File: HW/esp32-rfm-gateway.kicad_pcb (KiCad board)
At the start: 2 copper layers, 99 x 93.5 mm, 66 parts, among them J1 Res, J2 Boot, J20 220V~, J21 c5V, J22 s14500, J23 s18650, J24 cPS, J25 c3V3, J3 PinDbg, J30 AntSMA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

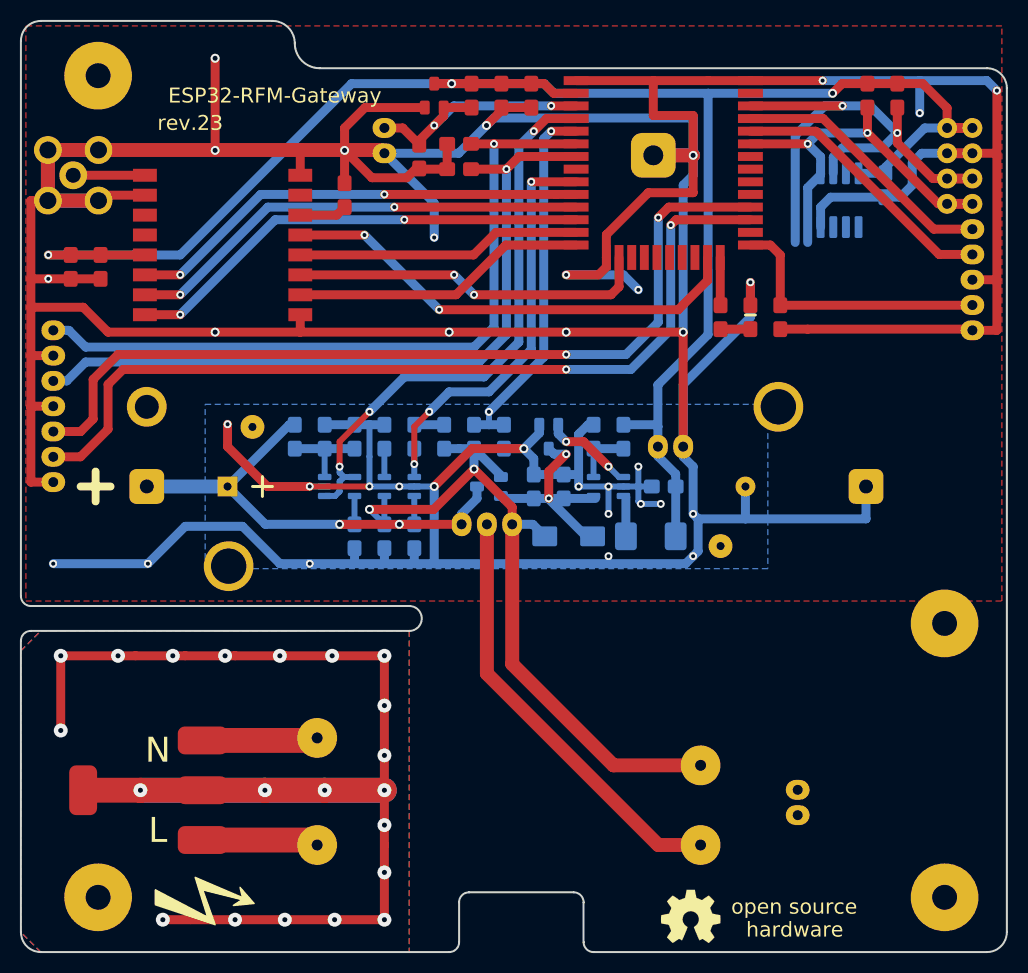
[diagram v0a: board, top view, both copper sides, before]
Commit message: Adds 4 LEDs, resistor and light pipes. The LEDs are NOT controlled yet !
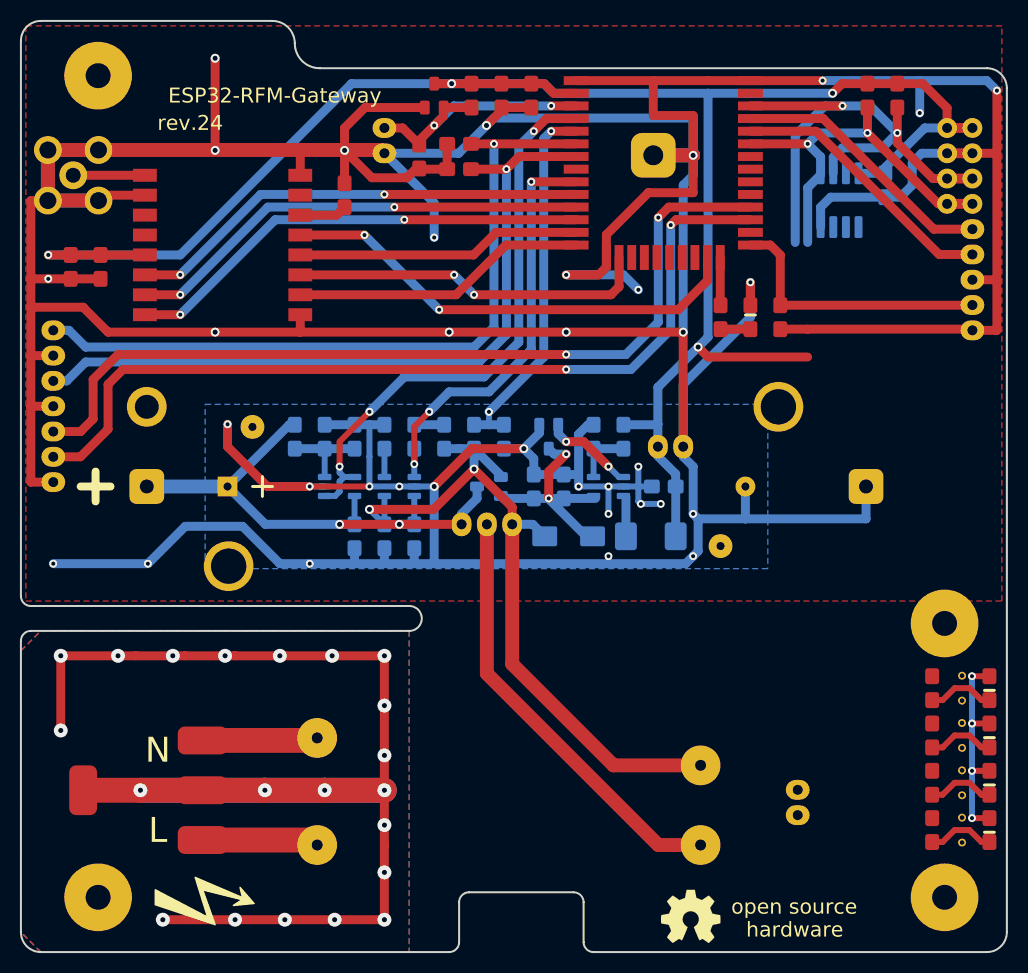
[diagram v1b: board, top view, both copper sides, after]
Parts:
- added D10: LED, CalinGeneric:LED0805HS, F.Cu at (133.2, 125.0)
- added D11: LED, CalinGeneric:LED0805HS, F.Cu at (133.2, 120.2)
- added D12: LED, CalinGeneric:LED0805HS, F.Cu at (133.2, 115.5)
- added D13: LED, CalinGeneric:LED0805HS, F.Cu at (133.2, 110.8)
- added R10: 100, CalinGeneric:R0805HS, F.Cu at (127.5, 125.0)
- added R11: 100, CalinGeneric:R0805HS, F.Cu at (127.5, 120.2)
- added R12: 100, CalinGeneric:R0805HS, F.Cu at (127.5, 115.5)
- added R13: 100, CalinGeneric:R0805HS, F.Cu at (127.5, 110.8)
- added SYM10: LightPipe, CalinGeneric:SLP3-xxx-150-x, F.Cu at (130.5, 125.0)
- added SYM11: LightPipe, CalinGeneric:SLP3-xxx-150-x, F.Cu at (130.5, 120.2)
- added SYM12: LightPipe, CalinGeneric:SLP3-xxx-150-x, F.Cu at (130.5, 115.5)
- added SYM13: LightPipe, CalinGeneric:SLP3-xxx-150-x, F.Cu at (130.5, 110.8)
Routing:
- net +3V3: track 190.1 -> 222.7 mm, vias 3 -> 8
- net Net-(D13-PadK): track 0.00 -> 6.74 mm
- net Net-(D12-PadK): track 0.00 -> 6.74 mm
- net Net-(D11-PadK): track 0.00 -> 6.74 mm
- net Net-(D10-PadK): track 0.00 -> 6.74 mm
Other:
- board text added: "rev.24"
- board text removed: "rev.23"

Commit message: Changes to schematic to a hierarchical one
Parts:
- J1: value Res -> ph_1x2
- J2: value Boot -> ph_1x2
- J21: value c5V -> ph_1x2
- J24: value cPS -> ph_1x3
- J25: value c3V3 -> ph_1x2
- J3: value PinDbg -> ph_1x3
- J4, J5: value PinsI2C -> ph_1x4
- J6: value PinsUSART2 -> ph_1x3
- J7: value ExtButtons -> ph_1x4
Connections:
- net /ACL renamed /Power Section/ACL
- net /ACN renamed /Power Section/ACN
- net /PwrSW renamed /Power Section/PwrSW
- net /VinReg renamed /Power Section/VinReg

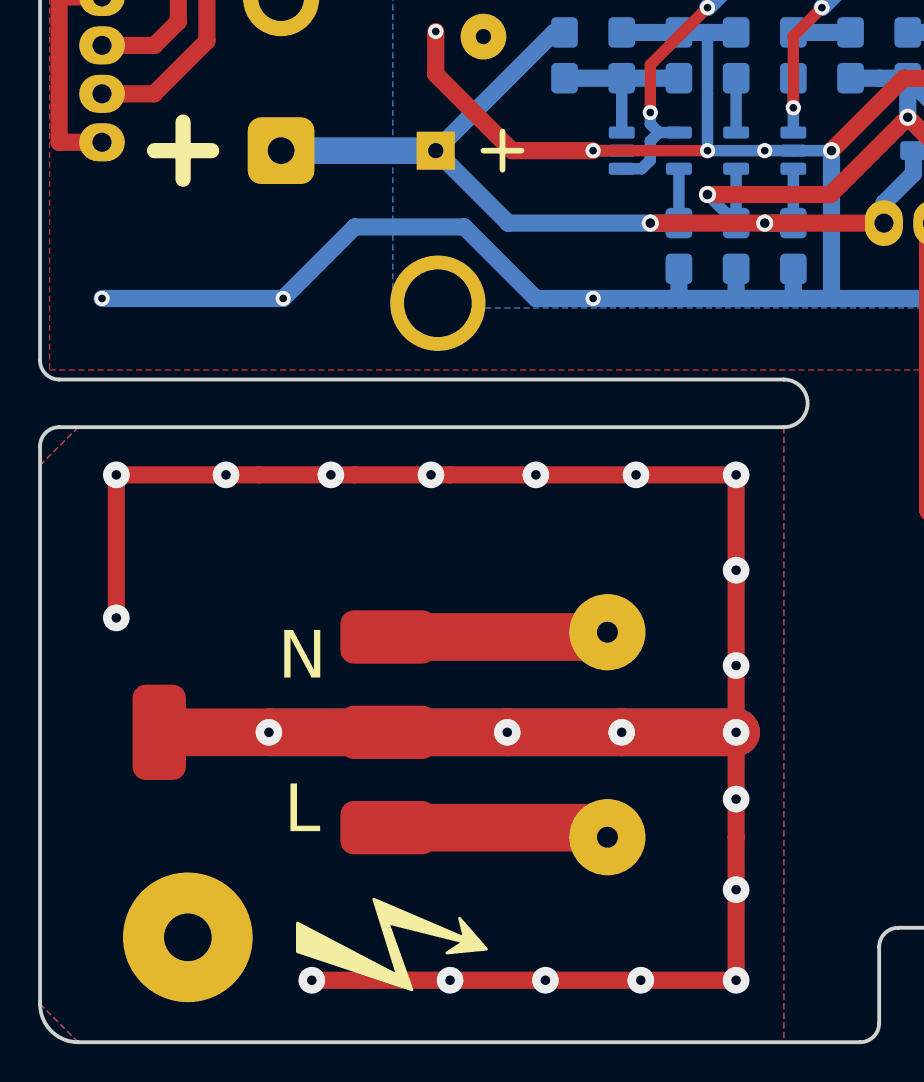
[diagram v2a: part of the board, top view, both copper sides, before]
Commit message: Changes the high-voltage section
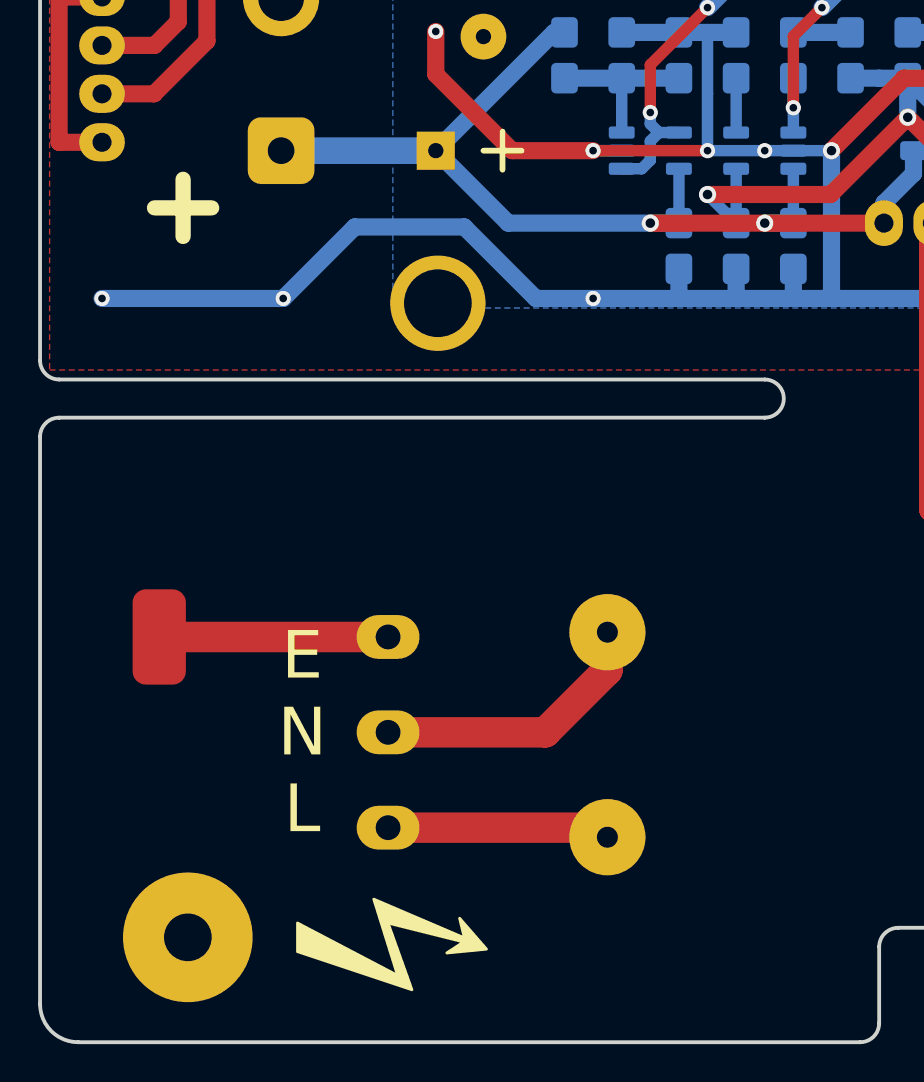
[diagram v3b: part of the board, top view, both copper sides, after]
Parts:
- J20: footprint CalinConnectors:SMD_Pins_Big_1x3 -> CalinConnectors:THT_Pins_Big_1x3
- moved H5 5.00 mm to (42.2, 116.0)
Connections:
- J20 pad 1: /Power Section/ACN -> Earth
- J20 pad 2: Earth -> /Power Section/ACN
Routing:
- net Earth: track 143.5 -> 12.0 mm, vias 21 -> 0
- net /Power Section/ACN: track 11.6 -> 14.8 mm
- removed copper zone on B.Cu, net Earth
- removed copper zone on F.Cu, net Earth
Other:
- outline, holes or cut-outs redrawn
- board text added: "E N L"
- board text removed: "N L"

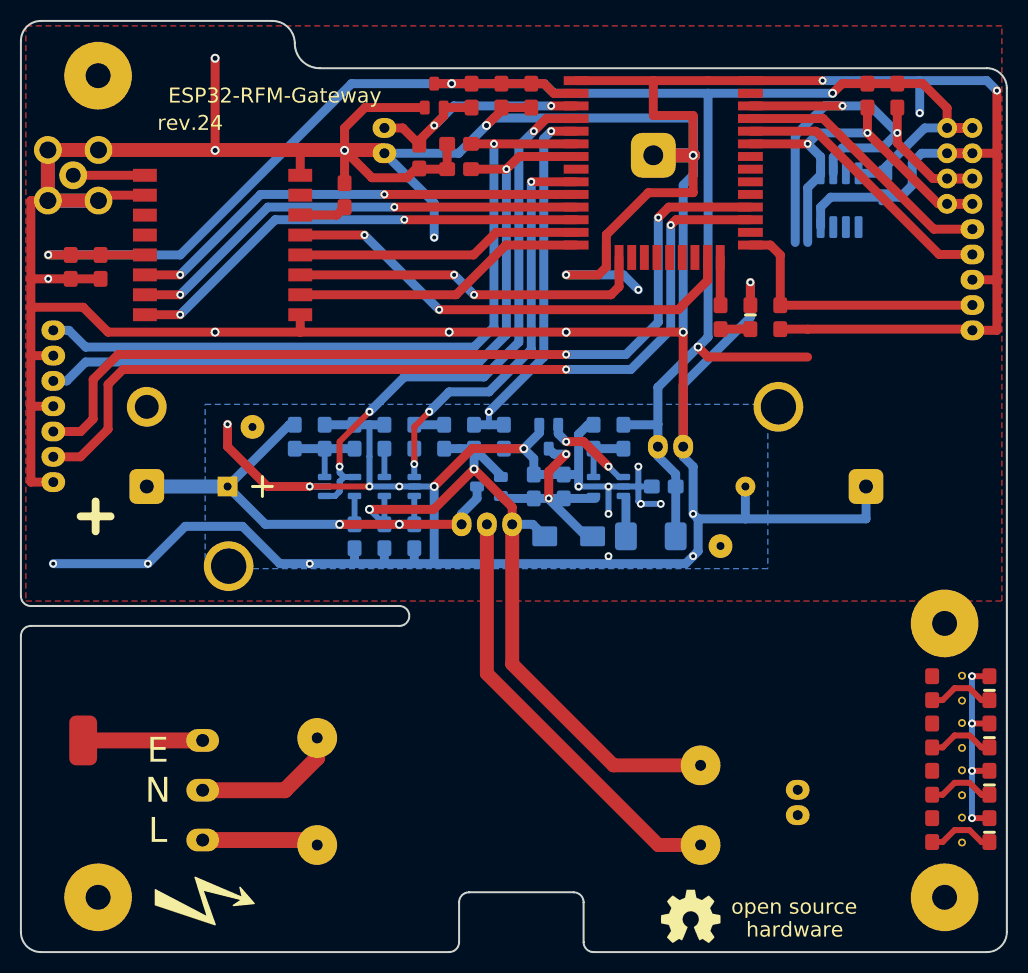
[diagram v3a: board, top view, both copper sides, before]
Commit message: Adds DTR and RTS connector and the components for automatic setting of EN and Boot signals
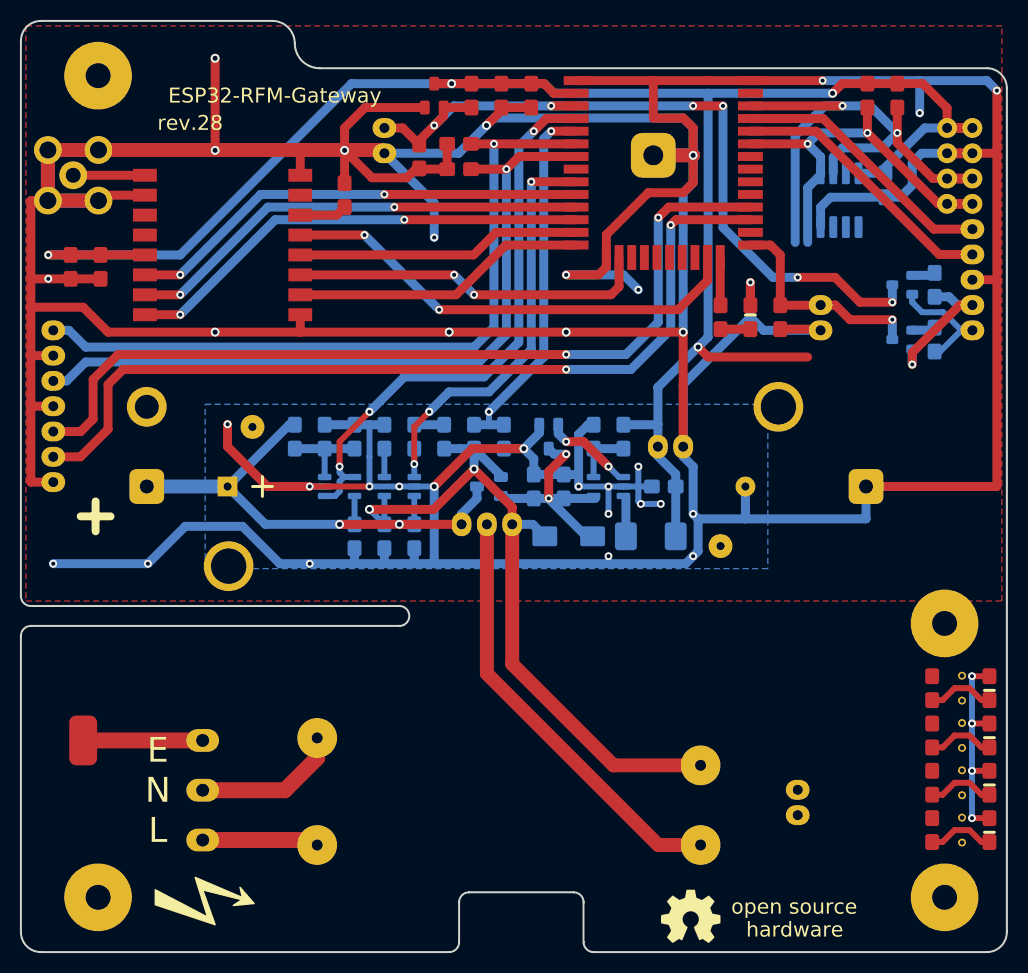
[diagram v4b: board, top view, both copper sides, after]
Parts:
- added J40: ph_1x2, CalinConnectors:Pin_Header_Straight_1x02, F.Cu at (131.5, 72.3)
- added Q40: BC817, CalinGeneric:SOT-23, B.Cu at (124.5, 70.2)
- added Q41: BC817, CalinGeneric:SOT-23, B.Cu at (124.5, 75.8)
- added R40: 10K, CalinGeneric:R0805HS, B.Cu at (127.8, 70.2)
- added R41: 10K, CalinGeneric:R0805HS, B.Cu at (127.8, 75.8)
- moved J2 15.2 mm to (116.3, 72.3)
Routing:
- net /Reset: track 26.8 -> 78.1 mm, vias 2 -> 6
- net GND: track 734.9 -> 751.9 mm
- net /Additional Modules/DTR: track 0.00 -> 14.9 mm, vias 0 -> 1
- net /Additional Modules/RTS: track 0.00 -> 11.6 mm
- net /Boot: track 27.8 -> 22.3 mm, vias 0 -> 1
- net Net-(Q41-Pad1): track 0.00 -> 2.35 mm
- net Net-(Q40-Pad1): track 0.00 -> 2.35 mm
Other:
- board text added: "rev.28"
- board text removed: "rev.24"

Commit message: Adds the I2C LED driver and more track tunning
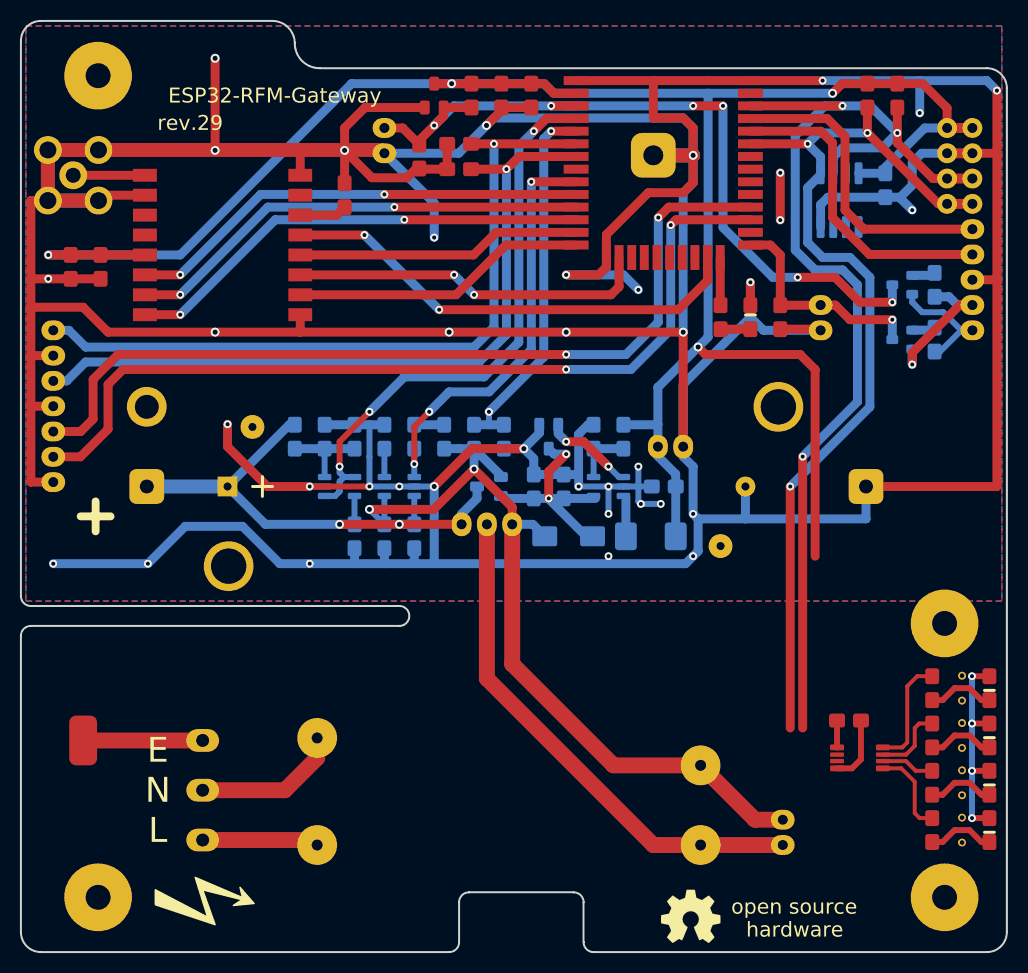
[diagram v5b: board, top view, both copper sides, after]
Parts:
- added C10: 100nF, CalinGeneric:C0805HS, F.Cu at (119.2, 114.0)
- added U10: PCA9633DP1, CalinGeneric:TSSOP8-SOT505-1-HS, F.Cu at (120.2, 117.8)
- moved J21 3.35 mm to (112.5, 124.0)
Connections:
- R10 pad 2: (no net) -> Net-(R10-Pad2)
- R11 pad 2: (no net) -> Net-(R11-Pad2)
- R12 pad 2: (no net) -> Net-(R12-Pad2)
- R13 pad 2: (no net) -> Net-(R13-Pad2)
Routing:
- net /SDA: track 39.2 -> 95.5 mm, vias 2 -> 3
- net /SCL: track 54.2 -> 109.5 mm, vias 2 -> 3
- net +3V3: track 222.7 -> 249.4 mm
- net GND: track 751.9 -> 769.8 mm, vias 35 -> 38
- net Net-(R13-Pad2): track 0.00 -> 11.2 mm
- net +5VP: track 74.2 -> 84.7 mm
- net Net-(R10-Pad2): track 0.00 -> 8.87 mm
- net Net-(R12-Pad2): track 0.00 -> 7.30 mm
- net Net-(R11-Pad2): track 0.00 -> 5.35 mm
- net /U0RXD: track 27.4 -> 31.8 mm
- net /U0TXD: track 26.9 -> 31.2 mm
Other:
- board text added: "rev.29"
- board text removed: "rev.28"

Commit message: Adds the HIH8xxx humidity and temperature sensor
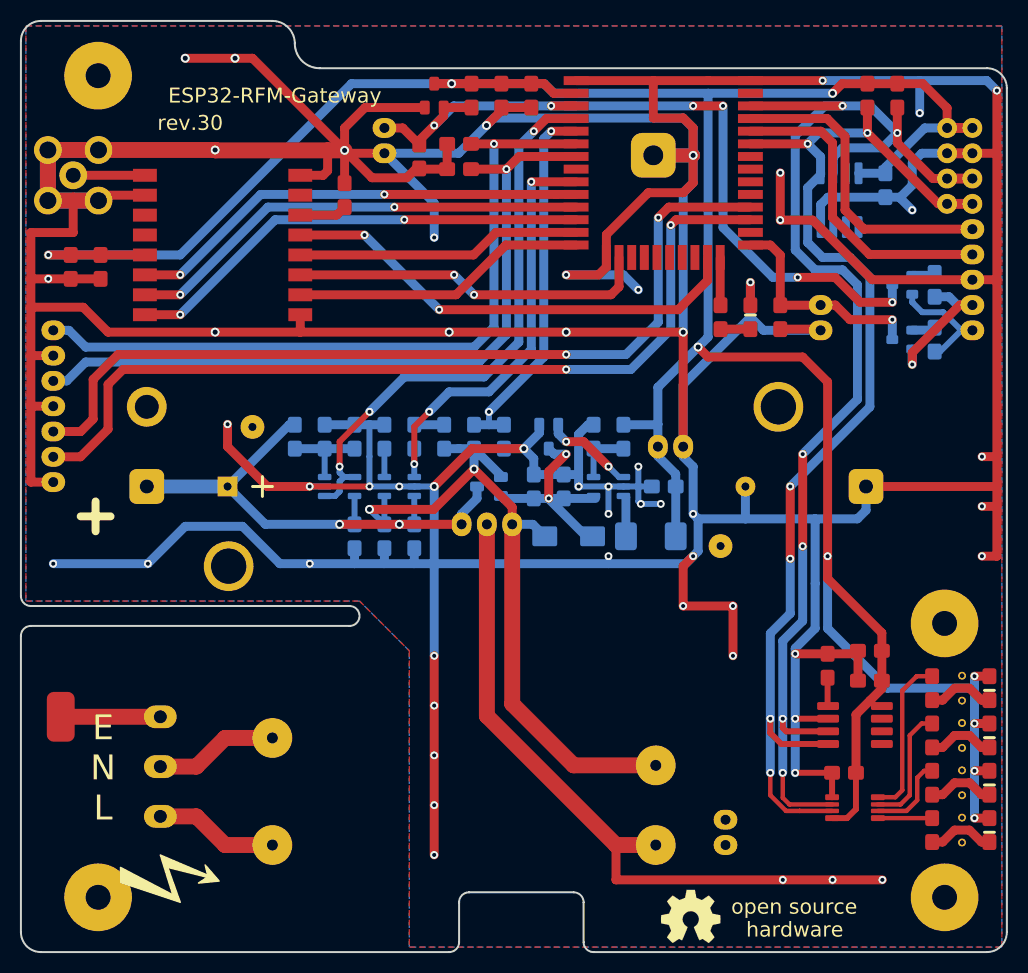
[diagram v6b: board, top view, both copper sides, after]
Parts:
- added C11: 1uF, CalinGeneric:C0805HS, F.Cu at (121.2, 107.0)
- added C41: 100nF, CalinGeneric:C0805HS, F.Cu at (117.0, 108.5)
- added C42: 100nF, CalinGeneric:C0805HS, F.Cu at (121.2, 110.0)
- added U41: HIH8000_I2C, CalinGeneric:SOIC-8-HS, F.Cu at (119.8, 114.5)
- moved J21 5.75 mm to (106.8, 124.0)
- moved C10 5.27 mm to (118.7, 119.2)
- moved U10 5.02 mm to (119.8, 122.8)
- moved J20 4.87 mm to (50.0, 118.6)
- moved SYM4 4.78 mm to (55.5, 121.2)
- moved U20 4.50 mm to (80.5, 117.2)
- moved SYM3 4.16 mm to (51.0, 130.0)
- moved H5 3.27 mm to (40.0, 113.6)
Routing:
- net GND: track 769.8 -> 925.0 mm, vias 38 -> 56
- net +3V3: track 249.4 -> 299.6 mm, vias 8 -> 9
- net /SDA: track 95.5 -> 117.6 mm, vias 3 -> 6
- net /SCL: track 109.5 -> 128.1 mm, vias 3 -> 6
- net +5VP: track 84.7 -> 72.1 mm
- net Net-(R13-Pad2): track 11.2 -> 16.3 mm
- net Net-(R12-Pad2): track 7.30 -> 12.3 mm
- net Net-(R10-Pad2): track 8.87 -> 5.45 mm
- net Net-(R11-Pad2): track 5.35 -> 8.44 mm
- net Net-(C41-Pad1): track 0.00 -> 2.87 mm
- net /Power Section/ACN: track 14.8 -> 12.4 mm
- net Earth: track 12.0 -> 10.0 mm
- net /Power Section/ACL: track 11.7 -> 12.4 mm
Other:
- outline, holes or cut-outs redrawn
- rule trace_min: 0.2 -> 0.25
- board text added: "rev.30"
- board text removed: "rev.29"
